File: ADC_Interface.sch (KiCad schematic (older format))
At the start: 18 parts

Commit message: Design Power (Dual Rail) section
Also add USB-C connection
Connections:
- net +3.3VA renamed +3.3VADC
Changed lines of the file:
@@
 U 1 1 5EE62AE8
 P 7900 4650
+AR Path="/5EE62AE8" Ref="FB?"  Part="1"
+AR Path="/5EE5ECAD/5EE62AE8" Ref="FB?"  Part="1"
 F 0 "FB?" V 7950 4750 50  0000 C CNN
 F 1 "BLM15HD102SN1" V 8050 4350 50  0001 C CNN
@@
 U 1 1 5EE62AEE
 P 7000 4250
+AR Path="/5EE62AEE" Ref="U?"  Part="1"
+AR Path="/5EE5ECAD/5EE62AEE" Ref="U?"  Part="1"
 F 0 "U?" H 6550 5100 50  0000 C CNN
 F 1 "ADS131M04" H 7450 5100 50  0000 C CNN
@@
 U 1 1 5EE62AFE
 P 8200 5300
+AR Path="/5EE62AFE" Ref="#PWR?"  Part="1"
+AR Path="/5EE5ECAD/5EE62AFE" Ref="#PWR?"  Part="1"
 F 0 "#PWR?" H 8200 5050 50  0001 C CNN
 F 1 "GNDD" H 8204 5145 50  0000 C CNN
@@
 U 1 1 5EE62B05
 P 7100 5400
+AR Path="/5EE62B05" Ref="#PWR?"  Part="1"
+AR Path="/5EE5ECAD/5EE62B05" Ref="#PWR?"  Part="1"
 F 0 "#PWR?" H 7100 5150 50  0001 C CNN
 F 1 "GNDD" H 7150 5250 50  0000 C CNN
@@
 U 1 1 5EE62B0C
 P 6900 5400
+AR Path="/5EE62B0C" Ref="#PWR?"  Part="1"
+AR Path="/5EE5ECAD/5EE62B0C" Ref="#PWR?"  Part="1"
 F 0 "#PWR?" H 6900 5150 50  0001 C CNN
 F 1 "GNDA" H 6850 5250 50  0000 C CNN
@@
 U 1 1 5EE62B13
 P 7750 4550
+AR Path="/5EE62B13" Ref="R?"  Part="1"
+AR Path="/5EE5ECAD/5EE62B13" Ref="R?"  Part="1"
 F 0 "R?" V 7650 4450 50  0000 C CNN
 F 1 "27" V 7650 4550 50  0000 C CNN
@@
 U 1 1 5EE62B19
 P 8050 4550
+AR Path="/5EE62B19" Ref="FB?"  Part="1"
+AR Path="/5EE5ECAD/5EE62B19" Ref="FB?"  Part="1"
 F 0 "FB?" V 8000 4450 50  0000 C CNN
 F 1 "Ferrite_Bead_Small" V 7904 4550 50  0001 C CNN
@@
 U 1 1 5EE62B25
 P 4550 1600
+AR Path="/5EE62B25" Ref="C?"  Part="1"
+AR Path="/5EE5ECAD/5EE62B25" Ref="C?"  Part="1"
 F 0 "C?" H 4642 1691 50  0000 L CNN
 F 1 "220n" H 4642 1600 50  0000 L CNN
@@
 U 1 1 5EE62B2C
 P 7800 5000
+AR Path="/5EE62B2C" Ref="C?"  Part="1"
+AR Path="/5EE5ECAD/5EE62B2C" Ref="C?"  Part="1"
 F 0 "C?" H 7892 5091 50  0000 L CNN
 F 1 "220n" H 7892 5000 50  0000 L CNN
@@
 U 1 1 5EE62B35
 P 1250 1350
+AR Path="/5EE62B35" Ref="FB?"  Part="1"
+AR Path="/5EE5ECAD/5EE62B35" Ref="FB?"  Part="1"
 F 0 "FB?" V 1013 1350 50  0000 C CNN
 F 1 "Ferrite_Bead_Small" V 1104 1350 50  0001 C CNN
@@
 U 1 1 5EE62B3C
 P 2250 1600
+AR Path="/5EE62B3C" Ref="C?"  Part="1"
+AR Path="/5EE5ECAD/5EE62B3C" Ref="C?"  Part="1"
 F 0 "C?" H 2342 1691 50  0000 L CNN
 F 1 "100n" H 2342 1600 50  0000 L CNN
@@
 U 1 1 5EE62B43
 P 1500 1600
+AR Path="/5EE62B43" Ref="C?"  Part="1"
+AR Path="/5EE5ECAD/5EE62B43" Ref="C?"  Part="1"
 F 0 "C?" H 1592 1691 50  0000 L CNN
 F 1 "220n" H 1592 1600 50  0000 L CNN
@@
 U 1 1 5EE62B4A
 P 3000 1600
+AR Path="/5EE62B4A" Ref="C?"  Part="1"
+AR Path="/5EE5ECAD/5EE62B4A" Ref="C?"  Part="1"
 F 0 "C?" H 3092 1691 50  0000 L CNN
 F 1 "10n" H 3092 1600 50  0000 L CNN
@@
 U 1 1 5EE62B51
 P 5300 1600
+AR Path="/5EE62B51" Ref="C?"  Part="1"
+AR Path="/5EE5ECAD/5EE62B51" Ref="C?"  Part="1"
 F 0 "C?" H 5392 1691 50  0000 L CNN
 F 1 "10n" H 5392 1600 50  0000 L CNN
@@
 U 1 1 5EE62B58
 P 8600 5000
+AR Path="/5EE62B58" Ref="C?"  Part="1"
+AR Path="/5EE5ECAD/5EE62B58" Ref="C?"  Part="1"
 F 0 "C?" H 8692 5091 50  0000 L CNN
 F 1 "10n" H 8692 5000 50  0000 L CNN
@@
 U 1 1 5EE62B66
 P 2250 1900
+AR Path="/5EE62B66" Ref="#PWR?"  Part="1"
+AR Path="/5EE5ECAD/5EE62B66" Ref="#PWR?"  Part="1"
 F 0 "#PWR?" H 2250 1650 50  0001 C CNN
 F 1 "GNDA" H 2255 1727 50  0000 C CNN
@@
 Wire Wire Line
 	1500 1800 1500 1700
-$Comp
-L power:+3.3VA #PWR?
-U 1 1 5EE62B7B
-P 2250 1250
-F 0 "#PWR?" H 2250 1100 50  0001 C CNN
-F 1 "+3.3VA" H 2265 1423 50  0000 C CNN
-F 2 "" H 2250 1250 50  0001 C CNN
-F 3 "" H 2250 1250 50  0001 C CNN
-	1    2250 1250
-	1    0    0    -1
-$EndComp
 Wire Wire Line
 	2250 1250 2250 1350
@@
 U 1 1 5EE62B82
 P 800 1250
+AR Path="/5EE62B82" Ref="#PWR?"  Part="1"
+AR Path="/5EE5ECAD/5EE62B82" Ref="#PWR?"  Part="1"
 F 0 "#PWR?" H 800 1100 50  0001 C CNN
 F 1 "+3V3" H 815 1423 50  0000 C CNN
@@
 U 1 1 5EE62B8A
 P 4950 1350
+AR Path="/5EE62B8A" Ref="#PWR?"  Part="1"
+AR Path="/5EE5ECAD/5EE62B8A" Ref="#PWR?"  Part="1"
 F 0 "#PWR?" H 4950 1200 50  0001 C CNN
 F 1 "+3V3" H 4965 1523 50  0000 C CNN
@@
 U 1 1 5EE62B95
 P 4950 1850
+AR Path="/5EE62B95" Ref="#PWR?"  Part="1"
+AR Path="/5EE5ECAD/5EE62B95" Ref="#PWR?"  Part="1"
 F 0 "#PWR?" H 4950 1600 50  0001 C CNN
 F 1 "GNDD" H 5000 1700 50  0000 C CNN
@@
 Connection ~ 4950 1800
 $Comp
-L power:+3.3VA #PWR?
-U 1 1 5EE62BA1
-P 6900 3250
-F 0 "#PWR?" H 6900 3100 50  0001 C CNN
-F 1 "+3.3VA" H 6750 3400 50  0000 C CNN
-F 2 "" H 6900 3250 50  0001 C CNN
-F 3 "" H 6900 3250 50  0001 C CNN
-	1    6900 3250
-	1    0    0    -1
-$EndComp
-$Comp
 L power:+3V3 #PWR?
 U 1 1 5EE62BA7
 P 7100 3250
+AR Path="/5EE62BA7" Ref="#PWR?"  Part="1"
+AR Path="/5EE5ECAD/5EE62BA7" Ref="#PWR?"  Part="1"
 F 0 "#PWR?" H 7100 3100 50  0001 C CNN
 F 1 "+3V3" H 7200 3400 50  0000 C CNN
@@
 U 1 1 5EE62BDA
 P 8650 4050
+AR Path="/5EE62BDA" Ref="R?"  Part="1"
+AR Path="/5EE5ECAD/5EE62BDA" Ref="R?"  Part="1"
 F 0 "R?" H 8709 4096 50  0000 L CNN
 F 1 "100k" H 8709 4005 50  0000 L CNN
@@
 U 1 1 5EE62BE2
 P 8450 3850
+AR Path="/5EE62BE2" Ref="#PWR?"  Part="1"
+AR Path="/5EE5ECAD/5EE62BE2" Ref="#PWR?"  Part="1"
 F 0 "#PWR?" H 8450 3700 50  0001 C CNN
 F 1 "+3V3" H 8465 4023 50  0000 C CNN
@@
 U 1 1 5EE62BF7
 P 3750 1600
+AR Path="/5EE62BF7" Ref="C?"  Part="1"
+AR Path="/5EE5ECAD/5EE62BF7" Ref="C?"  Part="1"
 F 0 "C?" H 3842 1691 50  0000 L CNN
 F 1 "0.1n" H 3842 1600 50  0000 L CNN
@@
 U 1 1 5EE62C03
 P 7700 3750
+AR Path="/5EE62C03" Ref="R?"  Part="1"
+AR Path="/5EE5ECAD/5EE62C03" Ref="R?"  Part="1"
 F 0 "R?" V 7650 3650 50  0000 C CNN
 F 1 "27" V 7700 3750 50  0000 C CNN
@@
 U 1 1 5EE62C09
 P 7700 3950
+AR Path="/5EE62C09" Ref="R?"  Part="1"
+AR Path="/5EE5ECAD/5EE62C09" Ref="R?"  Part="1"
 F 0 "R?" V 7650 3850 50  0000 C CNN
 F 1 "27" V 7700 3950 50  0000 C CNN
@@
 U 1 1 5EE62C0F
 P 8250 4050
+AR Path="/5EE62C0F" Ref="R?"  Part="1"
+AR Path="/5EE5ECAD/5EE62C0F" Ref="R?"  Part="1"
 F 0 "R?" H 8309 4096 50  0000 L CNN
 F 1 "100k" H 8309 4005 50  0000 L CNN
@@
 U 1 1 5EE62C19
 P 7700 3850
+AR Path="/5EE62C19" Ref="R?"  Part="1"
+AR Path="/5EE5ECAD/5EE62C19" Ref="R?"  Part="1"
 F 0 "R?" V 7650 3750 50  0000 C CNN
 F 1 "27" V 7700 3850 50  0000 C CNN
@@
 Text HLabel 8250 4650 2    50   Input ~ 0
 SYNC
+$Comp
+L power:+3.3VADC #PWR?
+U 1 1 5EF6ABF8
+P 2250 1250
+F 0 "#PWR?" H 2400 1200 50  0001 C CNN
+F 1 "+3.3VADC" H 2265 1423 50  0000 C CNN
+F 2 "" H 2250 1250 50  0001 C CNN
+F 3 "" H 2250 1250 50  0001 C CNN
+	1    2250 1250
+	1    0    0    -1
+$EndComp
+$Comp
+L power:+3.3VADC #PWR?
+U 1 1 5EF6B7F5
+P 6900 3250
+F 0 "#PWR?" H 7050 3200 50  0001 C CNN
+F 1 "+3.3VADC" H 6915 3423 50  0000 C CNN
+F 2 "" H 6900 3250 50  0001 C CNN
+F 3 "" H 6900 3250 50  0001 C CNN
+	1    6900 3250
+	1    0    0    -1
+$EndComp
 $EndSCHEMATC

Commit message: Design Mic. Board
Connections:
- net sheet5EE62ADB/ADC_N is gone; now on net ADC_0_N: U?.4 (AIN0N)
- net sheet5EE62ADB/ADC_P is gone; now on net ADC_0_P: U?.3 (AIN0P)
- net sheet5EE62ADC/ADC_N is gone; now on net ADC_1_N: U?.5 (AIN1N)
- net sheet5EE62ADC/ADC_P is gone; now on net ADC_1_P: U?.6 (AIN1P)
- net sheet5EE62ADD/ADC_N is gone; now on net ADC_2_N: U?.8 (AIN2N)
- net sheet5EE62ADD/ADC_P is gone; now on net ADC_2_P: U?.7 (AIN2P)
- net sheet5EE62ADE/ADC_N is gone; now on net ADC_3_N: U?.10 (AIN3P)
- net sheet5EE62ADE/ADC_P is gone; now on net ADC_3_P: U?.9 (AIN3N)

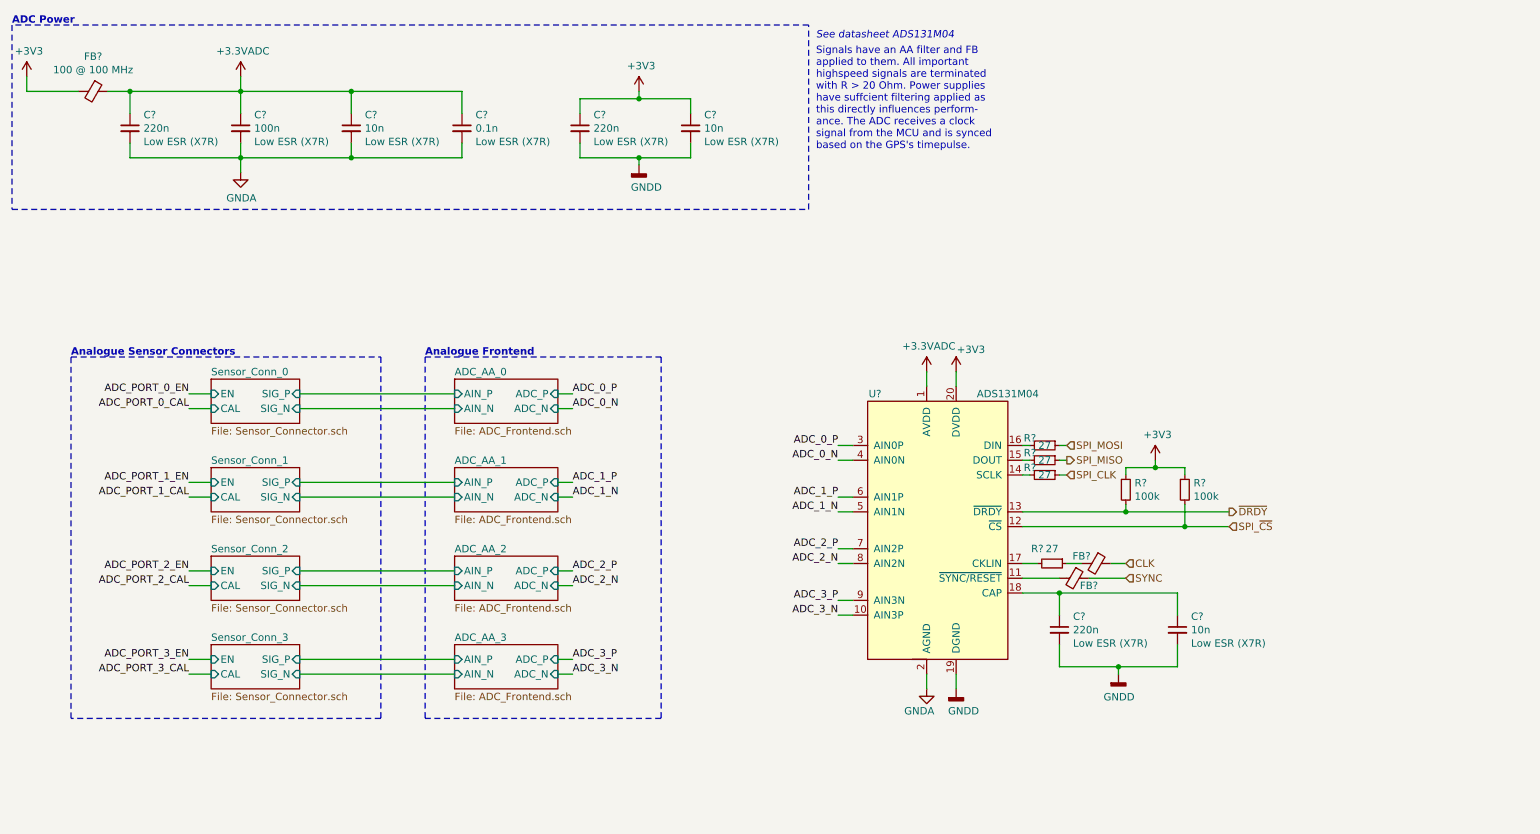
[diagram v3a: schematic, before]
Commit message: Change Connector Layout
Also add Mic. board to connectors
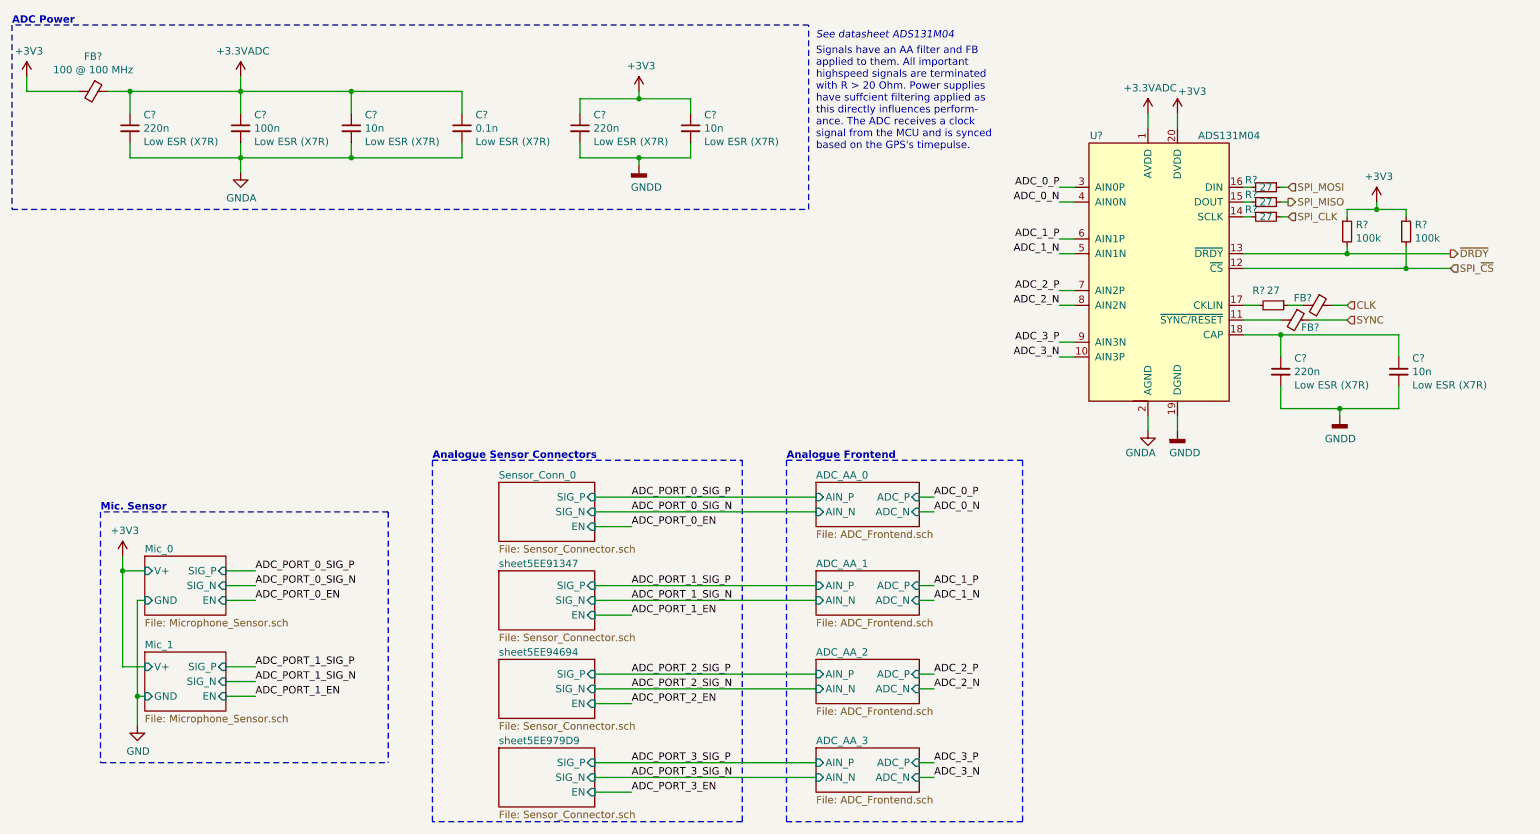
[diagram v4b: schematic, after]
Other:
- note added: "Mic. Sensor"
- moved on the sheet: C?, FB?, R?, U?

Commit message: Fix up some cap
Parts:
- removed C?: 0.1n, symbol Device:C_Small
- removed R?: 27, symbol Device:R_Small
- added C?: 10u, symbol Device:C_Small
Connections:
- net +3V3: now also C?.1
- net GND: now also C?.2
- net at U?.17 (CKLIN): now also FB?.2
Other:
- moved on the sheet: FB?
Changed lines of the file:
@@
 $Descr A4 11693 8268
 encoding utf-8
-Sheet 3 14
+Sheet 3 15
 Title ""
 Date ""
@@
 	0    1    1    0
 $EndComp
-Wire Wire Line
-	9150 2800 9050 2800
 $Comp
 L power:GNDD #PWR?
@@
 Wire Wire Line
 	8400 3650 8400 3550
-$Comp
-L Device:R_Small R?
-U 1 1 5EE62B13
-P 9250 2800
-AR Path="/5EE62B13" Ref="R?"  Part="1"
-AR Path="/5EE5ECAD/5EE62B13" Ref="R?"  Part="1"
-F 0 "R?" V 9150 2700 50  0000 C CNN
-F 1 "27" V 9150 2800 50  0000 C CNN
-F 2 "" H 9250 2800 50  0001 C CNN
-F 3 "~" H 9250 2800 50  0001 C CNN
-	1    9250 2800
-	0    1    1    0
-$EndComp
 $Comp
 L Device:Ferrite_Bead_Small FB?
@@
 	9750 2800 9650 2800
 Wire Wire Line
-	9450 2800 9350 2800
-Wire Wire Line
 	9300 2900 9050 2900
 Wire Wire Line
@@
 L Device:Ferrite_Bead_Small FB?
 U 1 1 5EE62B35
-P 1250 1350
+P 1200 1350
 AR Path="/5EE62B35" Ref="FB?"  Part="1"
 AR Path="/5EE5ECAD/5EE62B35" Ref="FB?"  Part="1"
-F 0 "FB?" V 1013 1350 50  0000 C CNN
-F 1 "Ferrite_Bead_Small" V 1104 1350 50  0001 C CNN
-F 2 "" V 1180 1350 50  0001 C CNN
-F 3 "~" H 1250 1350 50  0001 C CNN
-F 4 "100 @ 100 MHz" V 1104 1350 50  0000 C CNN "Notes"
-	1    1250 1350
+F 0 "FB?" V 963 1350 50  0000 C CNN
+F 1 "Ferrite_Bead_Small" V 1054 1350 50  0001 C CNN
+F 2 "" V 1130 1350 50  0001 C CNN
+F 3 "~" H 1200 1350 50  0001 C CNN
+F 4 "100 @ 100 MHz" V 1054 1350 50  0000 C CNN "Notes"
+	1    1200 1350
 	0    1    1    0
 $EndComp
@@
 Connection ~ 1500 1350
 Wire Wire Line
-	1500 1350 1350 1350
+	1500 1350 1300 1350
 Wire Wire Line
 	2250 1500 2250 1350
@@
 $EndComp
 Wire Wire Line
-	800  1250 800  1350
-Wire Wire Line
-	800  1350 1150 1350
+	800  1350 1100 1350
 $Comp
 L power:+3V3 #PWR?
@@
 	10450 2450 9750 2450
 Connection ~ 9750 2450
-$Comp
-L Device:C_Small C?
-U 1 1 5EE62BF7
-P 3750 1600
-AR Path="/5EE62BF7" Ref="C?"  Part="1"
-AR Path="/5EE5ECAD/5EE62BF7" Ref="C?"  Part="1"
-F 0 "C?" H 3842 1691 50  0000 L CNN
-F 1 "0.1n" H 3842 1600 50  0000 L CNN
-F 2 "" H 3750 1600 50  0001 C CNN
-F 3 "~" H 3750 1600 50  0001 C CNN
-F 4 "Low ESR (X7R)" H 3842 1509 50  0000 L CNN "Notes"
-	1    3750 1600
-	1    0    0    -1
-$EndComp
-Wire Wire Line
-	3750 1500 3750 1350
-Wire Wire Line
-	3750 1350 3000 1350
-Connection ~ 3000 1350
-Wire Wire Line
-	3000 1800 3750 1800
-Wire Wire Line
-	3750 1700 3750 1800
-Connection ~ 3000 1800
 $Comp
 L Device:R_Small R?
@@
 Text Notes 1300 4200 0    50   ~ 10
 Mic. Sensor
+$Comp
+L Device:C_Small C?
+U 1 1 5EF6EE7D
+P 800 1600
+AR Path="/5EF6EE7D" Ref="C?"  Part="1"
+AR Path="/5EE5ECAD/5EF6EE7D" Ref="C?"  Part="1"
+F 0 "C?" H 892 1691 50  0000 L CNN
+F 1 "10u" H 892 1600 50  0000 L CNN
+F 2 "" H 800 1600 50  0001 C CNN
+F 3 "~" H 800 1600 50  0001 C CNN
+F 4 "Low ESR (X7R)" H 892 1509 50  0000 L CNN "Notes"
+	1    800  1600
+	1    0    0    -1
+$EndComp
+$Comp
+L power:GND #PWR?
+U 1 1 5EF6F4F9
+P 800 1900
+F 0 "#PWR?" H 800 1650 50  0001 C CNN
+F 1 "GND" H 805 1727 50  0000 C CNN
+F 2 "" H 800 1900 50  0001 C CNN
+F 3 "" H 800 1900 50  0001 C CNN
+	1    800  1900
+	1    0    0    -1
+$EndComp
+Wire Wire Line
+	800  1900 800  1700
+Wire Wire Line
+	800  1250 800  1350
+Connection ~ 800  1350
+Wire Wire Line
+	800  1350 800  1500
+Wire Wire Line
+	9050 2800 9450 2800
 $EndSCHEMATC
